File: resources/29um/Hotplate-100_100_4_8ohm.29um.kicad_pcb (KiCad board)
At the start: 2 copper layers, 100 x 100 mm, 7 parts, among them J1 Hotplate_Power_Connection, J2 Hotplate_Power_Connection

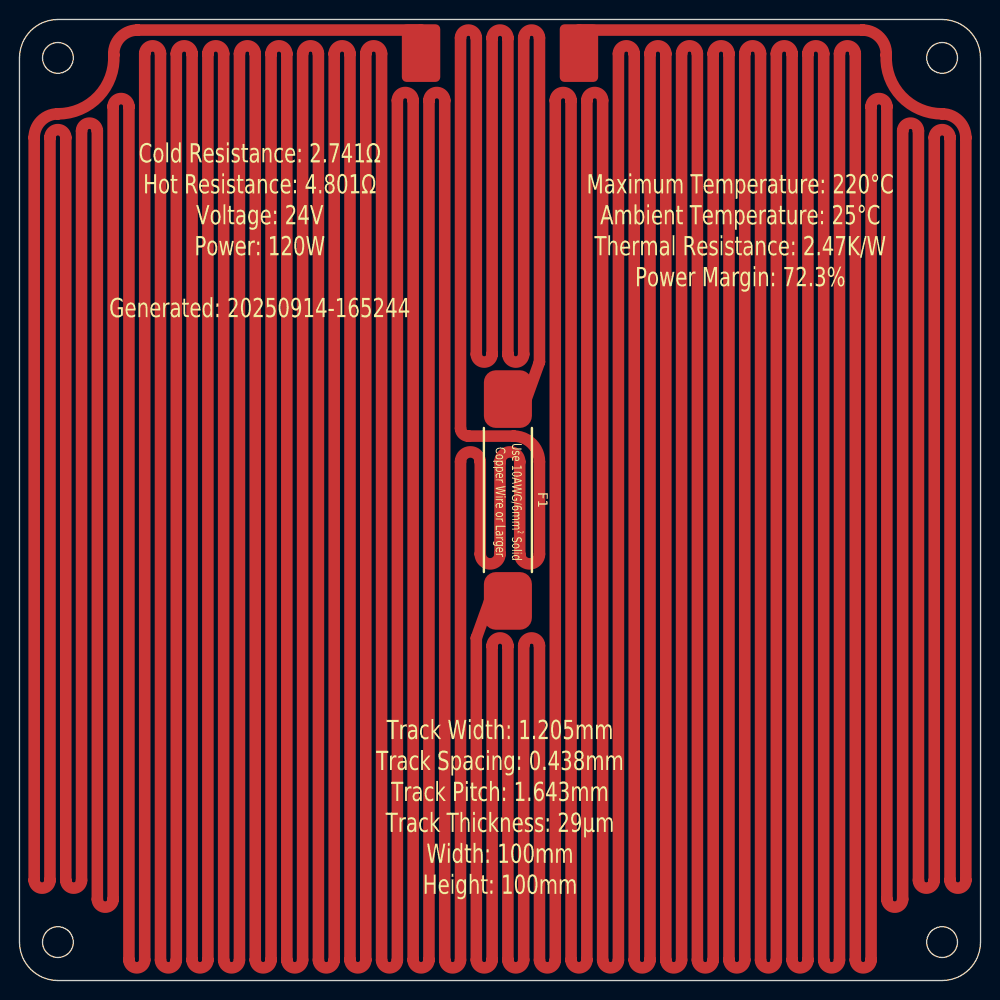
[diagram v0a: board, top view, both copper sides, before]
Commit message: Replaced obsolete 25mm thermal fuse footprint with new 35mm thermal fuse footprint.
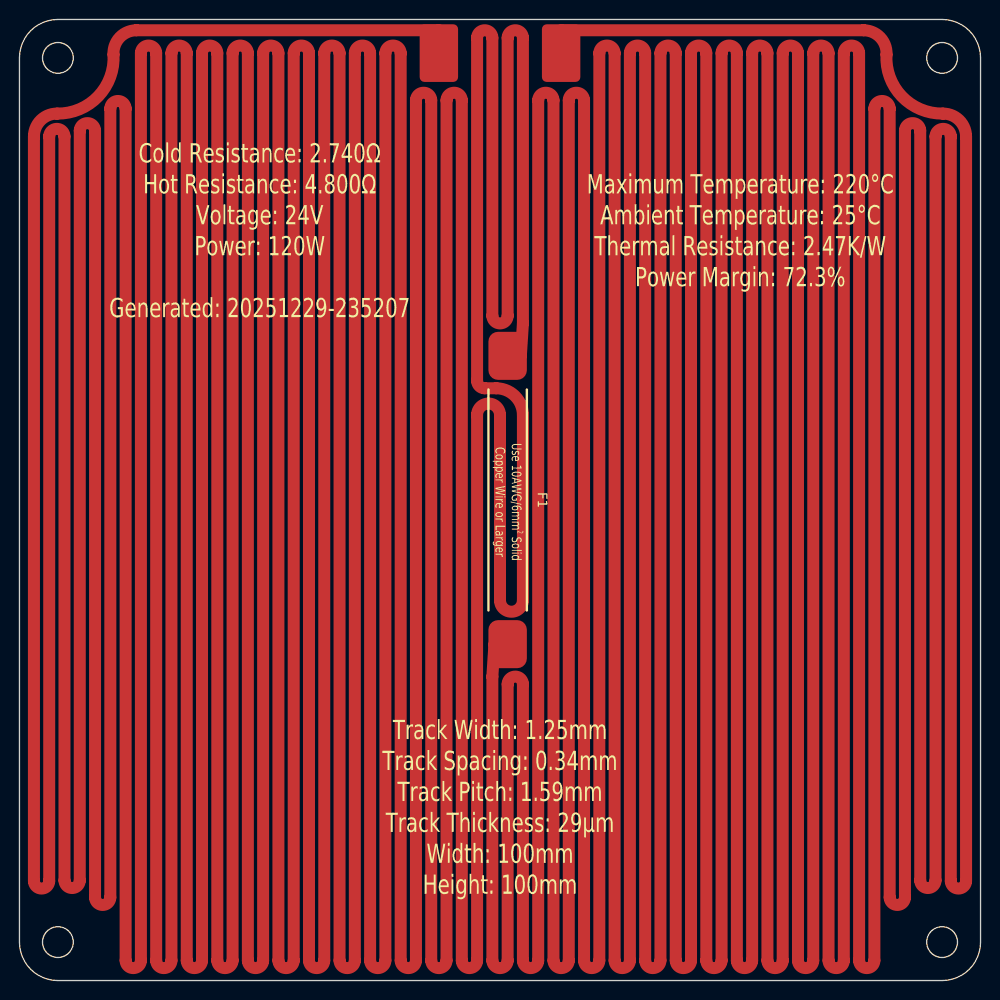
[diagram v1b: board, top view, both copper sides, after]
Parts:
- F1: footprint blg:Thermal Fuse, Front, 25mm -> blg:Thermal Fuse, SN100C, Front, 35mm
- moved J1 1.86 mm to (98.6, 58.5)
- moved J2 1.86 mm to (111.4, 58.5)
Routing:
- net Net-(J2-Pin_1): track 2718.4 -> 2830.0 mm
- net Net-(J1-Pin_1): track 2874.4 -> 2977.1 mm
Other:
- board text added: "Cold Resistance: 2.740Ω Hot Resistance: 4.800Ω Voltage: 24V Power: 120W Generated: 20251229-235207"
- board text added: "Track Width: 1.25mm Track Spacing: 0.34mm Track Pitch: 1.59mm Track Thickness: 29µm Width: 100mm Height: 100mm"
- board text removed: "Cold Resistance: 2.741Ω Hot Resistance: 4.801Ω Voltage: 24V Power: 120W Generated: 20250914-165244"
- board text removed: "Track Width: 1.205mm Track Spacing: 0.438mm Track Pitch: 1.643mm Track Thickness: 29µm Width: 100mm Height: 100mm"
